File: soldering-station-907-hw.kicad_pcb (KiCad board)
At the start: 2 copper layers, 132.7 x 56.5 mm, 41 parts, among them J1 DC in, J2 handle, Q1 IRFZ44N, Q2 PN2222A, Q3 PN2907A, Q4 PN2222A, SW1 PEC11R-4220F-S0024, U1 LM2596_regulator_module, U2 MCP602

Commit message: Routed.
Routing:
- net GNDD: track 75.8 -> 344.0 mm
- net +5VD: track 12.9 -> 171.6 mm
- net +24V: track 36.4 -> 113.9 mm
- net /R_BUTN_PIN: track 0.00 -> 55.8 mm
- net Net-(R6-Pad1): track 0.00 -> 53.3 mm
- net /R_MAIN_PIN: track 0.00 -> 43.6 mm
- net /LCD_DB4_PIN: track 0.00 -> 42.2 mm
- net /buzzerPIN: track 0.00 -> 39.0 mm
- net /R_SECD_PIN: track 0.00 -> 37.2 mm
- net /LCD_DB5_PIN: track 0.00 -> 34.4 mm
- net /LCD_DB6_PIN: track 0.00 -> 33.1 mm
- net /LCD_E_PIN: track 0.00 -> 31.5 mm
- net Net-(C3-Pad1): track 0.00 -> 29.1 mm
- net /LCD_RS_PIN: track 0.00 -> 28.1 mm
- net Net-(Q2-Pad2): track 0.00 -> 27.5 mm
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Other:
- net class PWR: clearance 0.254 -> 0.508; trace_width 0.508 -> 0.762; via_dia 1.27 -> 1.778; via_drill 0.889 -> 1.27

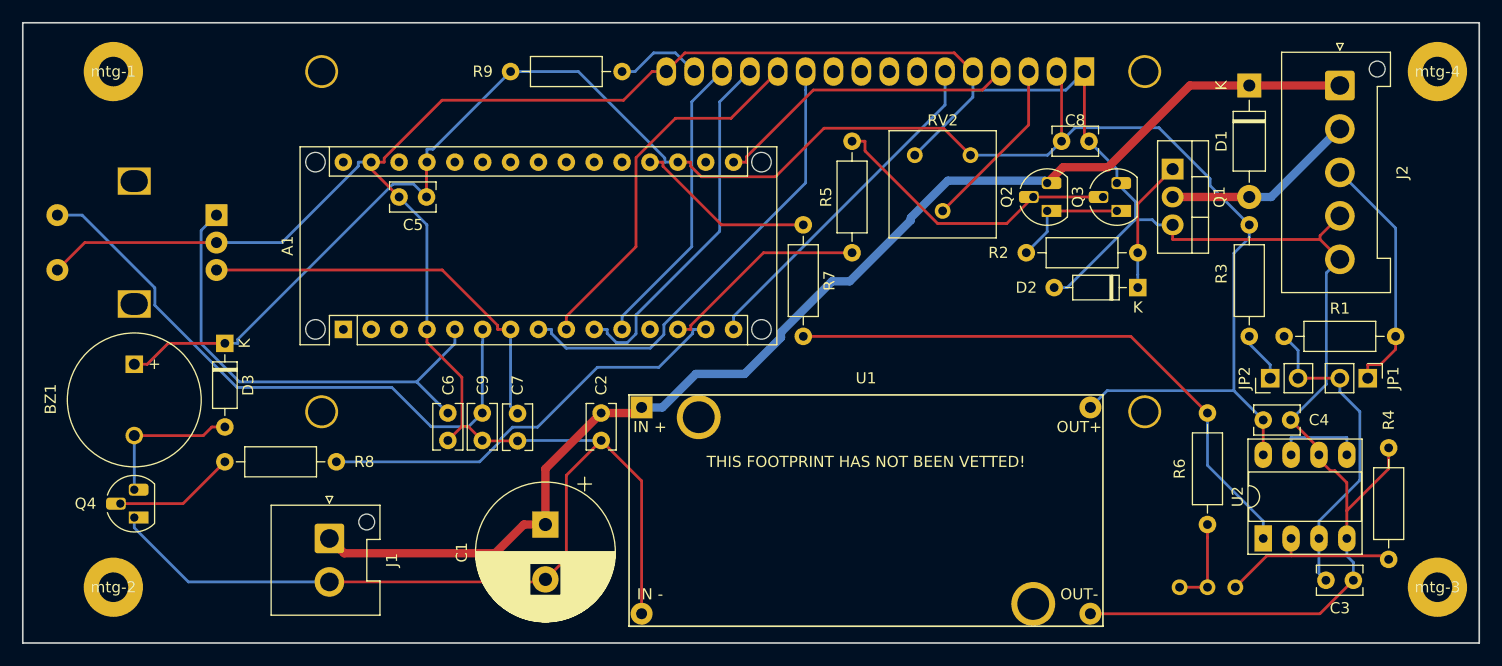
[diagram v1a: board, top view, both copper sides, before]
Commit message: Copper pours.
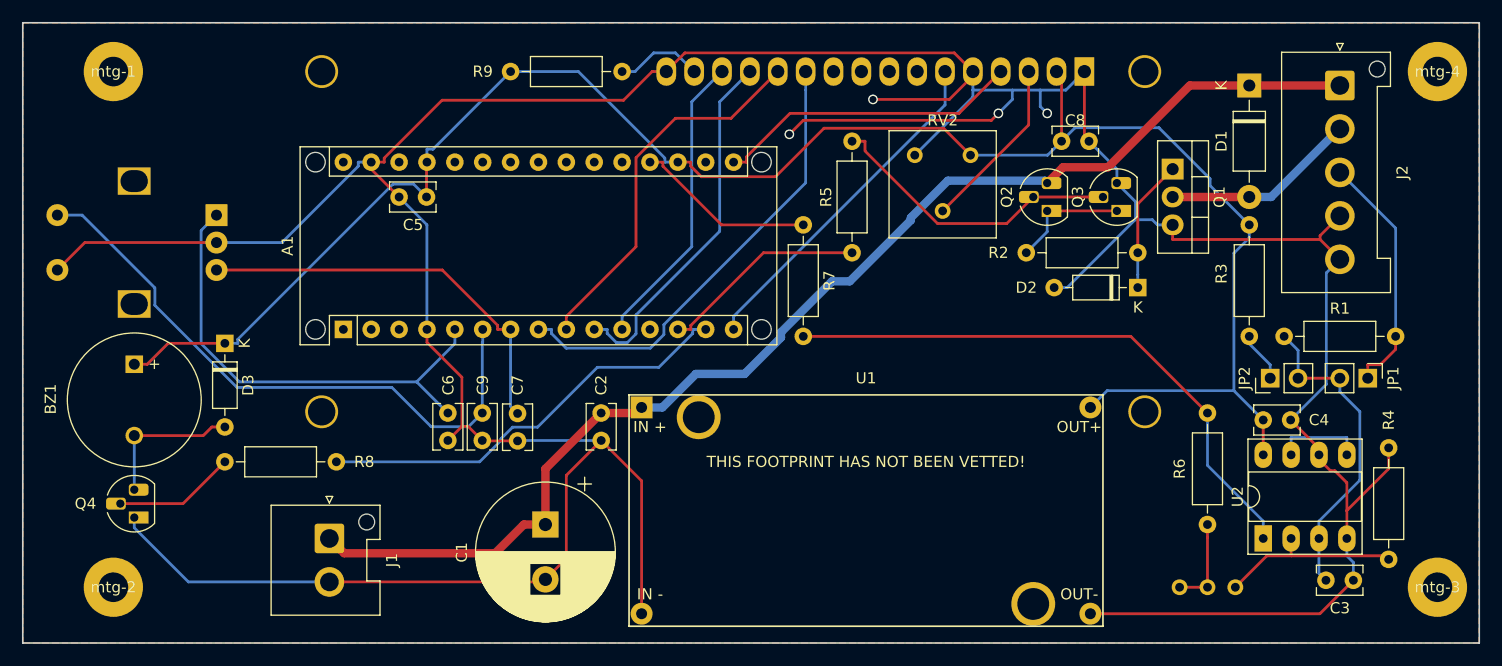
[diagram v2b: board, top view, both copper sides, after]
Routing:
- net GNDD: track 344.0 -> 379.3 mm, vias 0 -> 4
- added copper zone on B.Cu, net GNDD
- added copper zone on F.Cu, net GNDD
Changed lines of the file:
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@@
     (thickness 1.6)
     (drawings 4)
-    (tracks 287)
+    (tracks 304)
     (zones 0)
     (modules 41)
@@
   (title_block
     (title "Soldering Station 907")
-    (date 2019-07-24)
+    (date 2019-07-25)
     (rev v0.0.1)
     (company "Mithat Konar")
@@
   (segment (start 160.871 57.569) (end 160.871 56.9335) (width 0.254) (layer B.Cu) (net 7))
   (segment (start 171.031 55.245) (end 169.3425 56.9335) (width 0.254) (layer B.Cu) (net 7))
-  (segment (start 169.3425 56.9335) (end 160.871 56.9335) (width 0.254) (layer B.Cu) (net 7))
   (segment (start 160.871 55.245) (end 159.1696 53.5436) (width 0.254) (layer F.Cu) (net 7))
   (segment (start 159.1696 53.5436) (end 134.6324 53.5436) (width 0.254) (layer F.Cu) (net 7))
@@
   (segment (start 192.405 90.17) (end 192.405 89.575) (width 0.254) (layer F.Cu) (net 7))
   (segment (start 192.405 89.575) (end 189.825 86.995) (width 0.254) (layer F.Cu) (net 7))
+  (via (at 151.765 57.785) (size 0.889) (drill 0.635) (layers F.Cu B.Cu) (net 7))
+  (segment (start 158.331 57.785) (end 151.765 57.785) (width 0.254) (layer F.Cu) (net 7))
+  (segment (start 158.731 57.785) (end 158.331 57.785) (width 0.254) (layer F.Cu) (net 7))
+  (segment (start 160.871 55.245) (end 160.871 55.645) (width 0.254) (layer F.Cu) (net 7))
+  (segment (start 160.871 55.645) (end 158.731 57.785) (width 0.254) (layer F.Cu) (net 7))
+  (via (at 163.195 59.055) (size 0.889) (drill 0.635) (layers F.Cu B.Cu) (net 7))
+  (segment (start 164.465 56.9335) (end 164.465 57.785) (width 0.254) (layer B.Cu) (net 7))
+  (segment (start 164.465 57.785) (end 163.195 59.055) (width 0.254) (layer B.Cu) (net 7))
+  (segment (start 164.465 56.9335) (end 160.871 56.9335) (width 0.254) (layer B.Cu) (net 7))
+  (segment (start 167.005 56.9335) (end 167.005 58.42) (width 0.254) (layer B.Cu) (net 7))
+  (via (at 167.64 59.055) (size 0.889) (drill 0.635) (layers F.Cu B.Cu) (net 7))
+  (segment (start 167.005 56.9335) (end 164.465 56.9335) (width 0.254) (layer B.Cu) (net 7))
+  (segment (start 167.005 58.42) (end 167.64 59.055) (width 0.254) (layer B.Cu) (net 7))
+  (segment (start 169.3425 56.9335) (end 167.005 56.9335) (width 0.254) (layer B.Cu) (net 7))
+  (via (at 144.145 60.96) (size 0.889) (drill 0.635) (layers F.Cu B.Cu) (net 7))
+  (segment (start 145.415 59.69) (end 144.145 60.96) (width 0.254) (layer F.Cu) (net 7))
+  (segment (start 163.195 59.055) (end 162.56 59.69) (width 0.254) (layer F.Cu) (net 7))
+  (segment (start 162.56 59.69) (end 145.415 59.69) (width 0.254) (layer F.Cu) (net 7))
   (segment (start 110.1887 83.5187) (end 94.0281 83.5187) (width 0.254) (layer B.Cu) (net 9))
   (segment (start 94.0281 83.5187) (end 90.5504 80.041) (width 0.254) (layer B.Cu) (net 9))
@@
   (segment (start 139.065 77.5587) (end 158.331 58.2927) (width 0.254) (layer B.Cu) (net 27))
   (segment (start 158.331 58.2927) (end 158.331 55.245) (width 0.254) (layer B.Cu) (net 27))
-  (segment (start 139.065 63.5) (end 140.2463 63.5) (width 0.254) (layer F.Cu) (net 28))
-  (segment (start 163.411 55.245) (end 161.7296 56.9264) (width 0.254) (layer F.Cu) (net 28))
-  (segment (start 161.7296 56.9264) (end 146.3304 56.9264) (width 0.254) (layer F.Cu) (net 28))
-  (segment (start 146.3304 56.9264) (end 140.2463 63.0105) (width 0.254) (layer F.Cu) (net 28))
+  (segment (start 140.2463 63.5) (end 139.065 63.5) (width 0.254) (layer F.Cu) (net 28))
   (segment (start 140.2463 63.0105) (end 140.2463 63.5) (width 0.254) (layer F.Cu) (net 28))
+  (segment (start 144.2018 59.055) (end 140.2463 63.0105) (width 0.254) (layer F.Cu) (net 28))
+  (segment (start 163.411 55.245) (end 159.601 59.055) (width 0.254) (layer F.Cu) (net 28))
+  (segment (start 159.601 59.055) (end 144.2018 59.055) (width 0.254) (layer F.Cu) (net 28))
   (segment (start 92.71 87.63) (end 91.5287 87.63) (width 0.254) (layer F.Cu) (net 29))
   (segment (start 84.455 88.415) (end 90.7437 88.415) (width 0.254) (layer F.Cu) (net 29))
@@
   (segment (start 189.865 90.17) (end 189.865 88.5887) (width 0.254) (layer B.Cu) (net 48))
   (segment (start 189.865 88.5887) (end 194.945 88.5887) (width 0.254) (layer B.Cu) (net 48))
+  (zone (net 7) (net_name GNDD) (layer F.Cu) (hatch edge 0.508)
+    (connect_pads (clearance 0.508))
+    (min_thickness 0.254)
+    (fill yes (arc_segments 16) (thermal_gap 0.508) (thermal_bridge_width 0.508))
+    (polygon
+      (pts
+        (xy 74.295 50.8) (xy 207.01 50.8) (xy 207.01 107.315) (xy 74.295 107.315)
+      )
+    )
+  )
+  (zone (net 7) (net_name GNDD) (layer B.Cu) (hatch edge 0.508)
+    (connect_pads (clearance 0.508))
+    (min_thickness 0.254)
+    (fill yes (arc_segments 16) (thermal_gap 0.508) (thermal_bridge_width 0.508))
+    (polygon
+      (pts
+        (xy 74.295 50.8) (xy 207.01 50.8) (xy 207.01 107.315) (xy 74.295 107.315)
+      )
+    )
+  )
 )

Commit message: Silkscreen label.
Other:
- board text added: "mfk190725"
- board text added: "soldering station 907"
- board text added: "v0.0.1"
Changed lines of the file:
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@@
   (general
     (thickness 1.6)
-    (drawings 4)
+    (drawings 7)
     (tracks 304)
     (zones 0)
@@
     (descr "Through hole straight pin header, 1x02, 2.54mm pitch, single row")
     (tags "Through hole pin header THT 1x02 2.54mm single row")
-    (fp_text reference JP1 (at 0 -2.33 270) (layer F.SilkS)
+    (fp_text reference JP1 (at 0 -3.175) (layer F.SilkS)
       (effects (font (size 1.016 1.016) (thickness 0.1524)))
     )
@@
     (descr "Through hole straight pin header, 1x02, 2.54mm pitch, single row")
     (tags "Through hole pin header THT 1x02 2.54mm single row")
-    (fp_text reference JP2 (at 0 -2.33 90) (layer F.SilkS)
+    (fp_text reference JP2 (at 0 -3.175 180) (layer F.SilkS)
       (effects (font (size 1.016 1.016) (thickness 0.1524)))
     )
@@
     (descr "Resistor, Axial_DIN0207 series, Axial, Horizontal, pin pitch=10.16mm, 0.25W = 1/4W, length*diameter=6.3*2.5mm^2, http://cdn-reichelt.de/documents/datenblatt/B400/1_4W%23YAG.pdf")
     (tags "Resistor Axial_DIN0207 series Axial Horizontal pin pitch 10.16mm 0.25W = 1/4W length 6.3mm diameter 2.5mm")
-    (fp_text reference R3 (at 5.715 -2.54 90) (layer F.SilkS)
+    (fp_text reference R3 (at 5.08 -2.54 90) (layer F.SilkS)
       (effects (font (size 1.016 1.016) (thickness 0.1524)))
     )
@@
     (pad 1 thru_hole circle (at 0 0) (size 5.4 5.4) (drill 2.7) (layers *.Cu *.Mask))
   )
+  (gr_text v0.0.1 (at 76.2 62.23) (layer F.SilkS)
+    (effects (font (size 1.016 1.016) (thickness 0.1524)) (justify left))
+  )
+  (gr_text "soldering station 907" (at 76.2 60.325) (layer F.SilkS)
+    (effects (font (size 1.524 1.524) (thickness 0.3048)) (justify left))
+  )
+  (gr_text mfk190725 (at 75.565 102.235 90) (layer B.Cu)
+    (effects (font (size 1.016 1.016) (thickness 0.254)) (justify mirror))
+  )
   (gr_line (start 207.01 107.315) (end 207.01 50.8) (layer Edge.Cuts) (width 0.15))

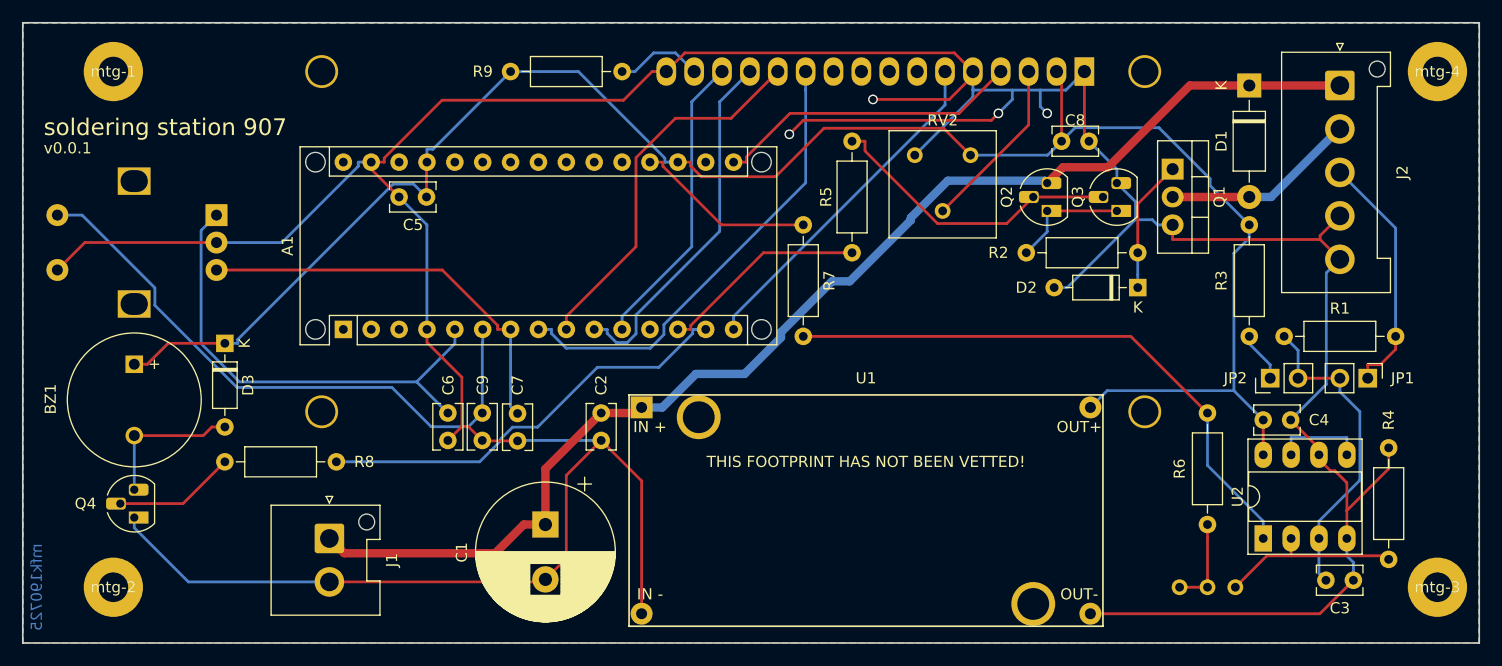
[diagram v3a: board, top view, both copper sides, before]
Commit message: Swapped R/L pins of SW1. Moved RV1 to front of board. Routing tweaks.
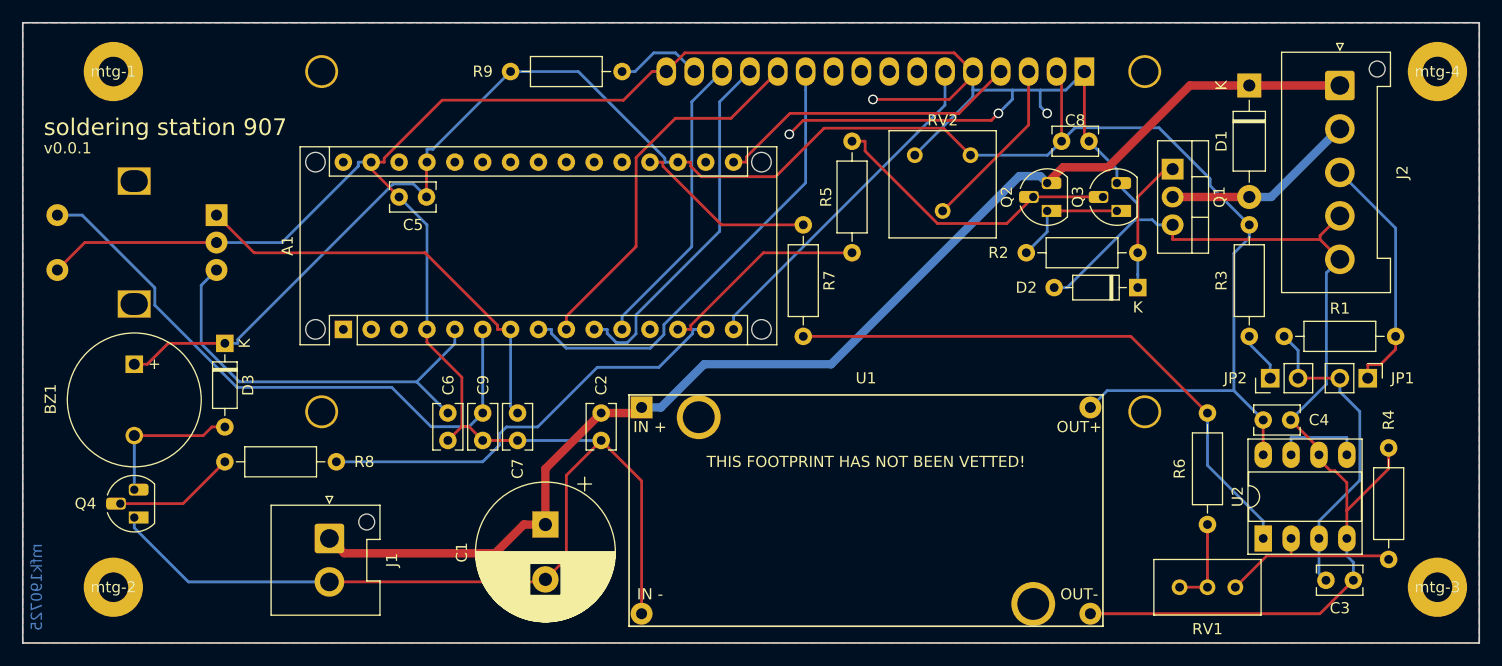
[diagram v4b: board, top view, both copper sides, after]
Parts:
- RV1: moved to F.Cu
- moved C7 2.54 mm to (119.4, 86.4), turned to 270 degrees
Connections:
- C7 pad 1: GNDD -> /R_SECD_PIN
- C7 pad 2: /R_SECD_PIN -> GNDD
- SW1 pad A: /R_MAIN_PIN -> /R_SECD_PIN
- SW1 pad B: /R_SECD_PIN -> /R_MAIN_PIN
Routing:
- net /R_MAIN_PIN: track 43.6 -> 38.6 mm
- net /R_SECD_PIN: track 37.2 -> 39.2 mm
- net /buzzerPIN: track 39.0 -> 39.5 mm
